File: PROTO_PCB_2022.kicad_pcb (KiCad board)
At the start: 2 copper layers, 81.4 x 40.6 mm, 30 parts, among them J1 HORN_EN1, J10 ECU_3, J11 12V_IN, J12 12V_OUT_EXTRA, J2 HORN_CONN, J3 STARTER_MOTOR_EN, J4 VESC_EN_SIGNAL, J5 ECU_POWER_DIST, J6 BRAKELIGHTS_EN1, J7 BRAKELIGHTS_CONN, J8 ECU_1, J9 ECU_2, Q1 HORN_MOSFET1, Q2 BRAKELIGHTS_MOSFET1, U1 LD1117S50TR_SOT223

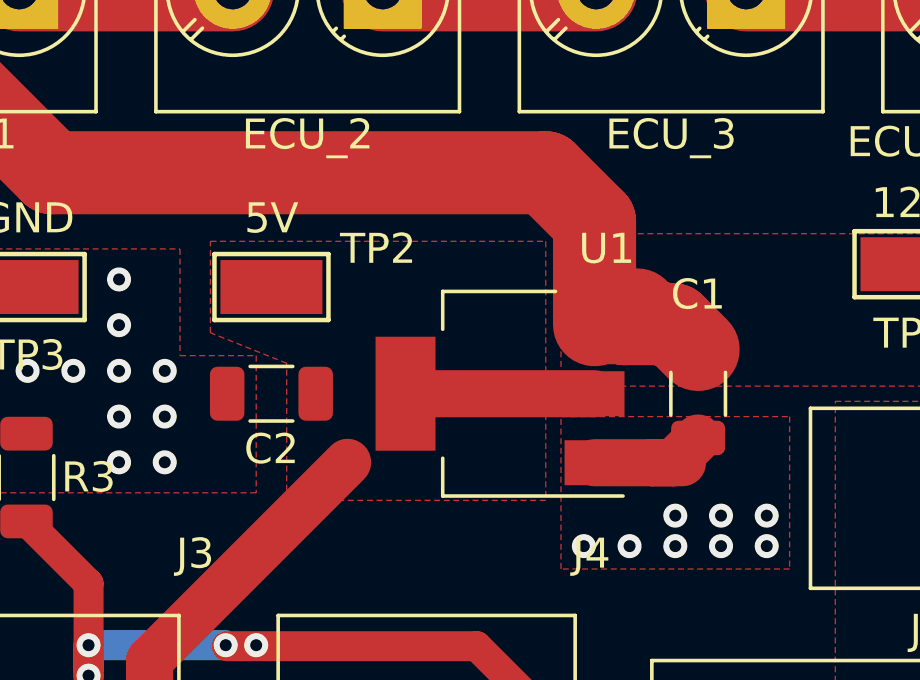
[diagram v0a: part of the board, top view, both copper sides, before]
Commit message: final design with gerbers
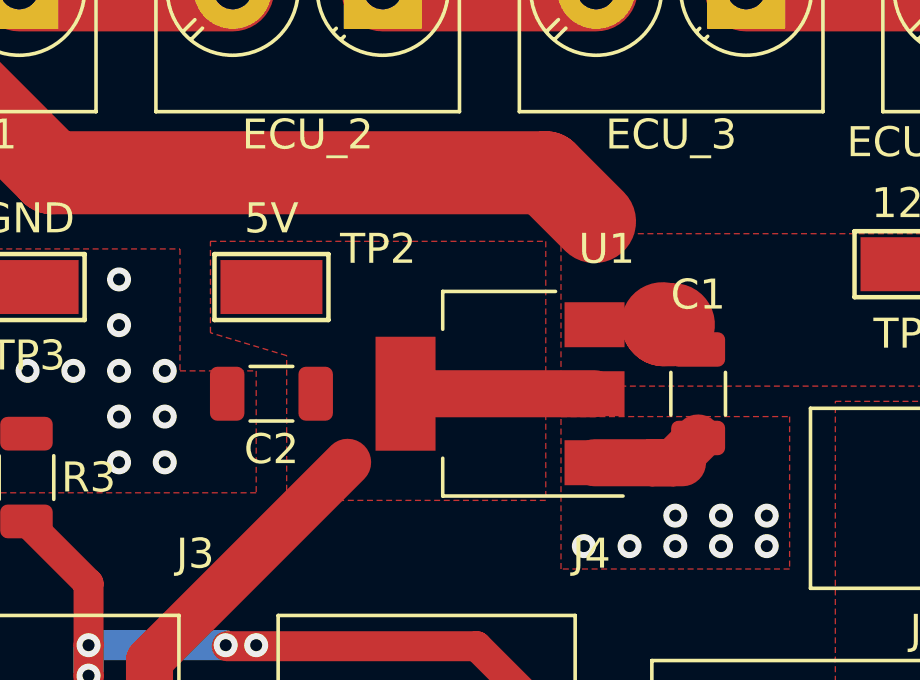
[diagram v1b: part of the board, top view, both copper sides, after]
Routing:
- net 12V_FOR_BRAKELIGHTS: track 68.5 -> 60.1 mm

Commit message: schematic done
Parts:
- removed the J1 at (95.5, 112.4)
- removed R5: 10k, Resistor_SMD:R_1206_3216Metric
- added F2: 5A, Fuse:Fuseholder_Blade_Mini_Keystone_3568, F.Cu at (84.4, 127.1)
- added F3: 2A, Fuse:Fuseholder_Blade_Mini_Keystone_3568, F.Cu at (84.4, 134.7)
- added F4: 2A, Fuse:Fuseholder_Blade_Mini_Keystone_3568, F.Cu at (105.9, 127.1)
- added F5: 1A, Fuse:Fuseholder_Blade_Mini_Keystone_3568, F.Cu at (84.4, 142.2)
- added F6: 1A, Fuse:Fuseholder_Blade_Mini_Keystone_3568, F.Cu at (105.9, 134.7)
- added F7: 1A, Fuse:Fuseholder_Blade_Mini_Keystone_3568, F.Cu at (84.4, 149.8)
- added H3: MountingHole, MountingHole:MountingHole_3.2mm_M3, F.Cu at (95.4, 158.2)
- added H4: MountingHole, MountingHole:MountingHole_3.2mm_M3, F.Cu at (95.4, 165.2)
- added J11: SW_START, Connector_Molex:Molex_Micro-Fit_3.0_43650-0200_1x02_P3.00mm_Horizontal, F.Cu at (149.2, 140.8)
- added J13: 5V_OUT_AUX, Connector_Molex:Molex_Micro-Fit_3.0_43650-0200_1x02_P3.00mm_Horizontal, F.Cu at (149.2, 154.3)
- D1, D2: footprint Resistor_SMD:R_0603_1608Metric -> LED_SMD:LED_1206_3216Metric
- F1: value Fuse -> 10A; footprint Fuse:Fuseholder_Blade_ATO_Littelfuse_Pudenz_2_Pin -> Fuse:Fuseholder_Blade_Mini_Keystone_3568
- H1, H2: footprint MountingHole:MountingHole_2.7mm_M2.5 -> MountingHole:MountingHole_3.2mm_M3
- J1: renamed from J11; value 12V_IN -> 12V_BATT; footprint TerminalBlock_Phoenix:TerminalBlock_Phoenix_PT-1,5-2-5.0-H_1x02_P5.00mm_Horizontal -> Connector_Molex:Molex_Micro-Fit_3.0_43650-0200_1x02_P3.00mm_Horizontal
- J10: value ECU_3 -> 12V_OUT_AUX; footprint TerminalBlock_Phoenix:TerminalBlock_Phoenix_PT-1,5-2-5.0-H_1x02_P5.00mm_Horizontal -> Connector_Molex:Molex_Micro-Fit_3.0_43650-0200_1x02_P3.00mm_Horizontal
- J12: value 12V_OUT_EXTRA -> VESC_START; footprint TerminalBlock_Phoenix:TerminalBlock_Phoenix_PT-1,5-2-5.0-H_1x02_P5.00mm_Horizontal -> Connector_Molex:Molex_Micro-Fit_3.0_43650-0200_1x02_P3.00mm_Horizontal
- J2: value HORN_CONN -> SW_KILL_DRIVER; footprint TerminalBlock_Phoenix:TerminalBlock_Phoenix_PT-1,5-2-5.0-H_1x02_P5.00mm_Horizontal -> Connector_Molex:Molex_Micro-Fit_3.0_43650-0200_1x02_P3.00mm_Horizontal
- J3: value STARTER_MOTOR_EN -> SW_KILL_LEFT; footprint footprints:436500201 -> Connector_Molex:Molex_Micro-Fit_3.0_43650-0200_1x02_P3.00mm_Horizontal
- J4: value VESC_EN_SIGNAL -> SW_KILL_RIGHT; footprint footprints:436500201 -> Connector_Molex:Molex_Micro-Fit_3.0_43650-0200_1x02_P3.00mm_Horizontal
- J5: value ECU_POWER_DIST -> ECU_POWER; footprint TerminalBlock_Phoenix:TerminalBlock_Phoenix_PT-1,5-2-5.0-H_1x02_P5.00mm_Horizontal -> Connector_Molex:Molex_Micro-Fit_3.0_43650-0200_1x02_P3.00mm_Horizontal
- J6: value BRAKELIGHTS_EN1 -> SW_BRAKE; footprint footprints:436500201 -> Connector_Molex:Molex_Micro-Fit_3.0_43650-0200_1x02_P3.00mm_Horizontal
- J7: value BRAKELIGHTS_CONN -> 12V_OUT_HORN; footprint TerminalBlock_Phoenix:TerminalBlock_Phoenix_PT-1,5-2-5.0-H_1x02_P5.00mm_Horizontal -> Connector_Molex:Molex_Micro-Fit_3.0_43650-0200_1x02_P3.00mm_Horizontal
- J8: value ECU_1 -> BRAKELIGHT_POWER; footprint TerminalBlock_Phoenix:TerminalBlock_Phoenix_PT-1,5-2-5.0-H_1x02_P5.00mm_Horizontal -> Connector_Molex:Molex_Micro-Fit_3.0_43650-0200_1x02_P3.00mm_Horizontal
- J9: value ECU_2 -> 12V_OUT_TEL; footprint TerminalBlock_Phoenix:TerminalBlock_Phoenix_PT-1,5-2-5.0-H_1x02_P5.00mm_Horizontal -> Connector_Molex:Molex_Micro-Fit_3.0_43650-0200_1x02_P3.00mm_Horizontal
- Q1: value HORN_MOSFET1 -> MOSFET_ECU
- Q2: value BRAKELIGHTS_MOSFET1 -> MOSFET_BRAKE_LIGHT
- R1: value 4.7k -> 1k
- R3: value 10k -> 1k
- R4: value 4.7k -> 10k
- moved J4 84.4 mm to (42.8, 141.6), turned to 0 degrees
- moved J1 82.7 mm to (208.7, 129.9)
- moved TP1 82.7 mm to (214.8, 112.6)
- moved J5 79.5 mm to (184.2, 151.6), turned to 0 degrees
- moved D2 77.5 mm to (101.0, 171.2), turned to 0 degrees
- moved Q2 75.9 mm to (111.2, 168.9)
- moved R4 75.9 mm to (92.2, 170.3), turned to 0 degrees
- moved J7 75.9 mm to (143.2, 127.3), turned to 0 degrees
- moved Q1 74.1 mm to (106.8, 168.9)
- moved J8 72.9 mm to (121.6, 155.9), turned to 0 degrees
- moved C2 72.6 mm to (185.3, 96.0)
- moved D1 72.0 mm to (97.0, 171.2), turned to 0 degrees
- moved R2 70.7 mm to (86.6, 169.9)
- moved J2 70.4 mm to (32.0, 121.5), turned to 0 degrees
- moved R1 69.9 mm to (81.0, 169.9), turned to 0 degrees
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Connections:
- C1 pad 1: 12V_FOR_BRAKELIGHTS -> +12V
- D1 pad 2: HORN_EN_5V -> Net-(D1-Pad2)
- D2 pad 2: BRAKELIGHTS_EN_5V -> Net-(D2-Pad2)
- F1 pad 1: BATT_12V -> +12V
- F1 pad 2: 12V_FOR_BRAKELIGHTS -> Net-(F1-Pad2)
- J1 pad 1: GND -> Net-(F1-Pad2)
- J1 pad 2: BATT_12V -> GND
- J10 pad 1: ECU_KILL_EN_TOGGLESWITCH_3B -> GND
- J10 pad 2: ECU_KILL_EN_TOGGLESWITCH_2B -> Net-(F6-Pad1)
- J12 pad 1: GND -> Net-(J11-Pad2)
- J12 pad 2: 12V_FOR_BRAKELIGHTS -> Net-(J11-Pad1)
- J2 pad 1: HORN_GND -> +5V
- J2 pad 2: 12V_FOR_BRAKELIGHTS -> Net-(J2-Pad2)
- J3 pad 1: VESC_EN_5V -> Net-(J2-Pad2)
- J3 pad 2: +5V -> Net-(J3-Pad2)
- J4 pad 1: GND -> Net-(J3-Pad2)
- J4 pad 2: VESC_EN_5V -> Net-(D1-Pad2)
- J5 pad 1: GND -> Net-(J5-Pad1)
- J5 pad 2: ECU_KILL_EN_TOGGLESWITCH_3B -> Net-(F2-Pad1)
- J6 pad 1: BRAKELIGHTS_EN_5V -> +5V
- J6 pad 2: +5V -> Net-(D2-Pad2)
- J7 pad 1: BRAKELIGHTS_GND -> GND
- J7 pad 2: 12V_FOR_BRAKELIGHTS -> Net-(F3-Pad1)
- J8 pad 1: ECU_KILL_EN_TOGGLESWITCH_1B -> Net-(J8-Pad1)
- J8 pad 2: 12V_FOR_BRAKELIGHTS -> Net-(F4-Pad1)
- J9 pad 1: ECU_KILL_EN_TOGGLESWITCH_2B -> GND
- J9 pad 2: ECU_KILL_EN_TOGGLESWITCH_1B -> Net-(F5-Pad1)
- Q1 pad 1: HORN_GND -> Net-(J5-Pad1)
- Q1 pad 2: HORN_EN_5V -> Net-(D1-Pad2)
- Q2 pad 1: BRAKELIGHTS_GND -> Net-(J8-Pad1)
- Q2 pad 2: BRAKELIGHTS_EN_5V -> Net-(D2-Pad2)
- R2 pad 1: HORN_EN_5V -> Net-(D1-Pad2)
- R3 pad 1: VESC_EN_5V -> Net-(D2-Pad1)
- R4 pad 1: Net-(D2-Pad1) -> Net-(D2-Pad2)
- TP1 pad 1: 12V_FOR_BRAKELIGHTS -> +12V
- U1 pad 3: 12V_FOR_BRAKELIGHTS -> +12V
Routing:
- net +5V: track 66.4 -> 0.00 mm
- net 12V_FOR_BRAKELIGHTS: track 60.1 -> 0.00 mm
- net HORN_EN_5V: track 31.6 -> 0.00 mm
- net BRAKELIGHTS_EN_5V: track 31.3 -> 0.00 mm, vias 4 -> 0
- net VESC_EN_5V: track 28.3 -> 0.00 mm, vias 4 -> 0
- net GND: track 21.3 -> 0.00 mm, vias 27 -> 0
- net BRAKELIGHTS_GND: track 15.2 -> 0.00 mm
- net HORN_GND: track 10.3 -> 0.00 mm
- net ECU_KILL_EN_TOGGLESWITCH_3B: track 7.12 -> 0.00 mm
- net ECU_KILL_EN_TOGGLESWITCH_2B: track 7.12 -> 0.00 mm
- net ECU_KILL_EN_TOGGLESWITCH_1B: track 7.12 -> 0.00 mm
- net Net-(D2-Pad1): track 4.33 -> 0.00 mm
- net Net-(D1-Pad1): track 4.25 -> 0.00 mm
- removed copper zone on F.Cu, net +5V
- removed copper zone on F.Cu, net 12V_FOR_BRAKELIGHTS
- removed copper zone on F.Cu, net BATT_12V
- removed copper zone on B.Cu, net GND
- removed copper zone on F.Cu, net GND
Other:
- board text removed: "5V"
- board text removed: "GND"
- board text removed: "HORN"
- board text removed: "LIGHTS"

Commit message: finished PCB layout
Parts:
- J1: footprint Connector_Molex:Molex_Micro-Fit_3.0_43650-0200_1x02_P3.00mm_Horizontal -> TerminalBlock_Phoenix:TerminalBlock_Phoenix_PT-1,5-2-5.0-H_1x02_P5.00mm_Horizontal
- moved J1 153.0 mm to (55.9, 121.8), turned to 270 degrees
- moved TP1 151.2 mm to (64.3, 127.0)
- moved H1 140.9 mm to (54.0, 104.0)
- moved F1 133.5 mm to (63.8, 138.2), turned to 180 degrees
- moved TP3 108.3 mm to (64.3, 120.1)
- moved J5 83.5 mm to (111.6, 110.2)
- moved J7 82.3 mm to (62.7, 110.2)
- moved J2 77.3 mm to (107.2, 139.7), turned to 180 degrees
- moved H3 74.1 mm to (146.0, 104.0)
- moved J10 72.9 mm to (86.1, 110.2)
- moved J9 68.2 mm to (74.4, 110.2)
- moved J13 67.7 mm to (97.8, 110.2)
- moved R4 66.1 mm to (146.6, 132.6), turned to 270 degrees
- moved C1 57.1 mm to (137.9, 122.2)
- moved H4 54.1 mm to (146.0, 146.0)
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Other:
- board size 81.4 x 40.6 mm -> 100 x 50 mm

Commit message: did some more layout work
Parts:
- removed F6, F7: 1A, Fuse:Fuseholder_Blade_Mini_Keystone_3568
- removed J10: 12V_OUT_AUX, Connector_Molex:Molex_Micro-Fit_3.0_43650-0200_1x02_P3.00mm_Horizontal
- removed J13: 5V_OUT_AUX, Connector_Molex:Molex_Micro-Fit_3.0_43650-0200_1x02_P3.00mm_Horizontal
- J9: value 12V_OUT_TEL -> 12V_OUT_AUX
- moved R2 49.5 mm to (112.5, 121.9), turned to 0 degrees
- moved R3 45.0 mm to (97.0, 129.0), turned to 90 degrees
- moved Q1 44.9 mm to (112.3, 117.6)
- moved R4 33.8 mm to (112.8, 132.1), turned to 180 degrees
- moved Q2 28.5 mm to (112.5, 127.0)
- moved TP3 26.4 mm to (59.2, 146.1), turned to 270 degrees
- moved F1 26.0 mm to (57.1, 113.0), turned to 270 degrees
- moved R1 24.9 mm to (84.6, 129.2), turned to 270 degrees
- moved C2 23.5 mm to (123.4, 118.6)
- moved J5 22.7 mm to (88.9, 110.0)
- moved F2 22.4 mm to (92.5, 118.6)
- moved J8 21.8 mm to (101.3, 110.0)
- moved F4 21.6 mm to (104.6, 118.4)
- moved TP1 21.3 mm to (58.7, 106.4), turned to 270 degrees
- moved J12 20.8 mm to (114.0, 110.0)
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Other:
- board size 100 x 50 mm -> 80 x 50 mm

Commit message: even more layout changes
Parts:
- removed F1: 10A, Fuse:Fuseholder_Blade_Mini_Keystone_3568
- added D3: LED, LED_SMD:LED_1206_3216Metric, F.Cu at (144.8, 116.1)
- added R5: 1k, Resistor_SMD:R_1206_3216Metric, F.Cu at (144.7, 119.4)
- moved TP3 34.6 mm to (58.4, 111.5)
- moved J1 8.89 mm to (56.1, 122.9)
- moved TP1 7.01 mm to (53.8, 111.5)
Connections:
- J1 pad 1: Net-(F1-Pad2) -> +12V
- J11 pad 2: Net-(J11-Pad2) -> Net-(D3-Pad2)
- J12 pad 1: Net-(J11-Pad2) -> Net-(J12-Pad1)

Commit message: finishes schematic, footprint assignment, and BOM
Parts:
- removed C1: 1u, Capacitor_SMD:C_1206_3216Metric
- removed C2: 4.7u, Capacitor_SMD:C_1206_3216Metric
- removed the TP2 at (125.7, 112.8)
- removed U1: LD1117S50TR_SOT223, Package_TO_SOT_SMD:SOT-223-3_TabPin2
- added F5: 1A, Fuse:Fuseholder_Blade_Mini_Keystone_3568, F.Cu at (185.7, 132.6)
- added J10: 12V_AUX, Connector_Molex:Molex_Micro-Fit_3.0_43650-0200_1x02_P3.00mm_Horizontal, F.Cu at (186.2, 148.4)
- added L2: RED, LED_SMD:LED_1206_3216Metric, F.Cu at (202.3, 131.8)
- added R1: 1k, Resistor_SMD:R_1206_3216Metric, F.Cu at (184.7, 152.0)
- J1: value 12V_BATT -> 12V_IN; footprint TerminalBlock_Phoenix:TerminalBlock_Phoenix_PT-1,5-2-5.0-H_1x02_P5.00mm_Horizontal -> Footprint Library:MOLEX_2002411212
- J5: value ECU_POWER -> 12V_ECU
- J6: renamed from J7; value 12V_OUT_HORN -> 12V_HORN
- J8: renamed from J9; value 12V_OUT_AUX -> 12V_TEL
- J9: renamed from J8; value BRAKELIGHT_POWER -> 12V_BRAKE_LIGHT
- L1: renamed from D1; value LED -> GREEN
- L3: renamed from D2; value LED -> GREEN
- L4: renamed from D3; value LED -> GREEN
- Q1, Q2: footprint Package_TO_SOT_SMD:SOT-23 -> Package_TO_SOT_SMD:TO-252-3_TabPin2
- TP1: value TestPoint -> 12V Test
- TP2: renamed from TP3; value TestPoint -> GND Test
- moved J1 120.9 mm to (176.4, 135.4), turned to 0 degrees
- moved Q2 60.3 mm to (165.1, 97.5)
- moved Q1 43.4 mm to (154.7, 108.2)
- renumbered F2 to F1, F3 to F2, F5 to F3, J6 to J7, R1 to R2, R2 to R3, R3 to R4, R4 to R5, R5 to R6
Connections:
- J2 pad 1: +5V -> +12V
- J7 pad 1: +5V -> +12V

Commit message: new layout
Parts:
- R6: value 1k -> 100
- moved L2 150.5 mm to (52.5, 146.7)
- moved R1 132.5 mm to (52.5, 142.9), turned to 180 degrees
- moved J10 120.9 mm to (71.3, 111.0)
- moved J1 115.4 mm to (61.3, 126.4), turned to 270 degrees
- moved Q1 109.6 mm to (48.6, 135.9), turned to 180 degrees
- moved F5 104.9 mm to (81.7, 118.7), turned to 270 degrees
- moved R3 56.9 mm to (57.1, 134.6)
- moved Q2 54.9 mm to (115.3, 120.7)
- moved TP1 35.5 mm to (58.8, 146.7), turned to 0 degrees
- moved L1 34.0 mm to (57.0, 137.8)
- moved TP2 31.4 mm to (58.8, 142.9), turned to 0 degrees
- moved J5 29.1 mm to (59.8, 111.0)
- moved R2 24.2 mm to (61.3, 136.1), turned to 90 degrees
- moved L4 24.2 mm to (121.7, 123.2), turned to 270 degrees
- moved R6 23.2 mm to (121.7, 117.5), turned to 90 degrees
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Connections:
- Q1 pad 1: Net-(J5-Pad1) -> Net-(J4-Pad2)
- Q1 pad 2: Net-(J4-Pad2) -> Net-(J5-Pad1)
- Q2 pad 1: Net-(J9-Pad1) -> Net-(J7-Pad2)
- Q2 pad 2: Net-(J7-Pad2) -> Net-(J9-Pad1)
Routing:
- net Net-(J5-Pad1): track 0.00 -> 58.6 mm
- net GND: track 0.00 -> 42.5 mm, vias 0 -> 11
- net Net-(J11-Pad1): track 0.00 -> 33.3 mm
- net Net-(J7-Pad2): track 0.00 -> 26.8 mm
- net Net-(J9-Pad1): track 0.00 -> 24.2 mm
- net Net-(J4-Pad2): track 0.00 -> 19.0 mm
- net Net-(J11-Pad2): track 0.00 -> 16.1 mm
- net Net-(J3-Pad2): track 0.00 -> 8.66 mm
- net Net-(J2-Pad2): track 0.00 -> 8.45 mm
- net Net-(J12-Pad1): track 0.00 -> 7.58 mm
- net Net-(L2-Pad1): track 0.00 -> 3.84 mm
- net Net-(L3-Pad1): track 0.00 -> 3.23 mm
- net Net-(L1-Pad1): track 0.00 -> 3.02 mm
- net Net-(L4-Pad1): track 0.00 -> 2.85 mm
- added copper zone on F.Cu, net +12V
- added copper zone on B.Cu, net GND
- added copper zone on F.Cu, net Net-(F1-Pad1)
- added copper zone on F.Cu, net Net-(F2-Pad1)
- added copper zone on F.Cu, net Net-(F3-Pad1)
- added copper zone on F.Cu, net Net-(F4-Pad1)
- added copper zone on F.Cu, net Net-(F5-Pad1)
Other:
- board size 80 x 50 mm -> 90.8 x 50.2 mm
- board text added: "GND"

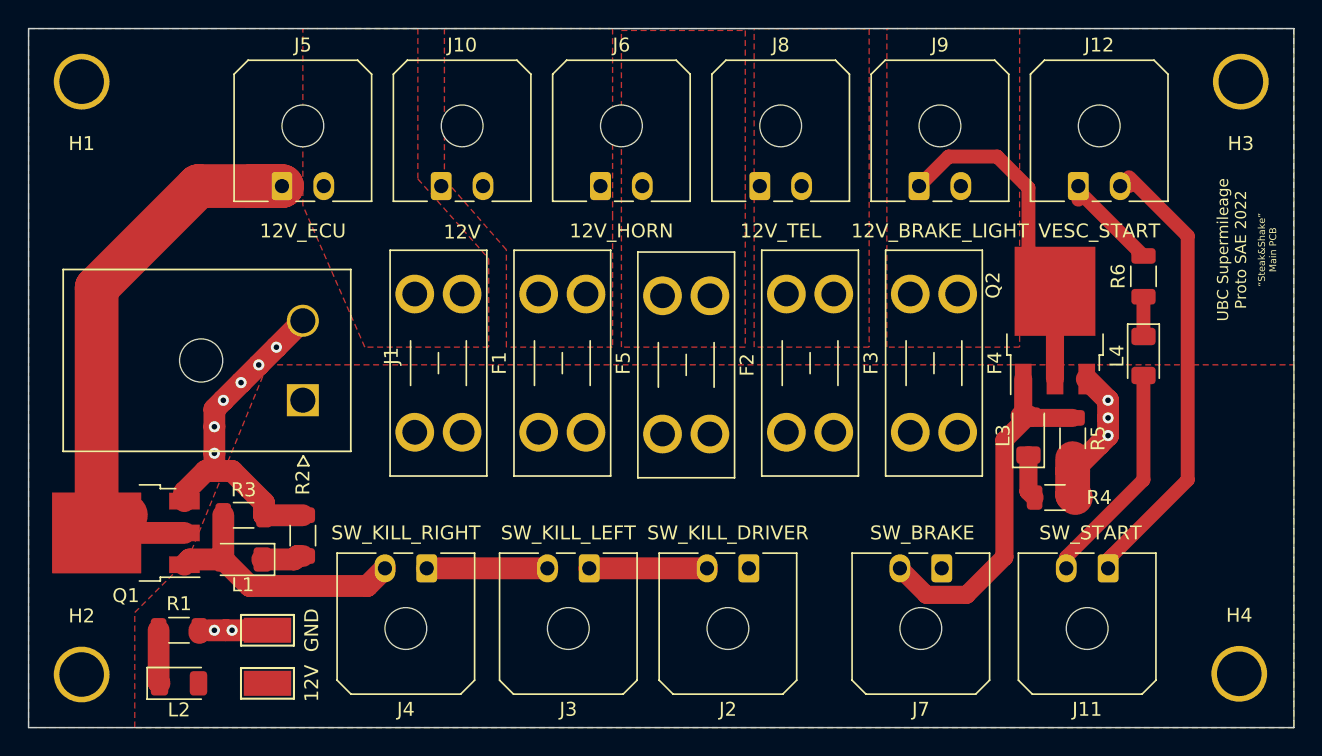
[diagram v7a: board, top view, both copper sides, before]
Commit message: updates silkscreen and minor tracing
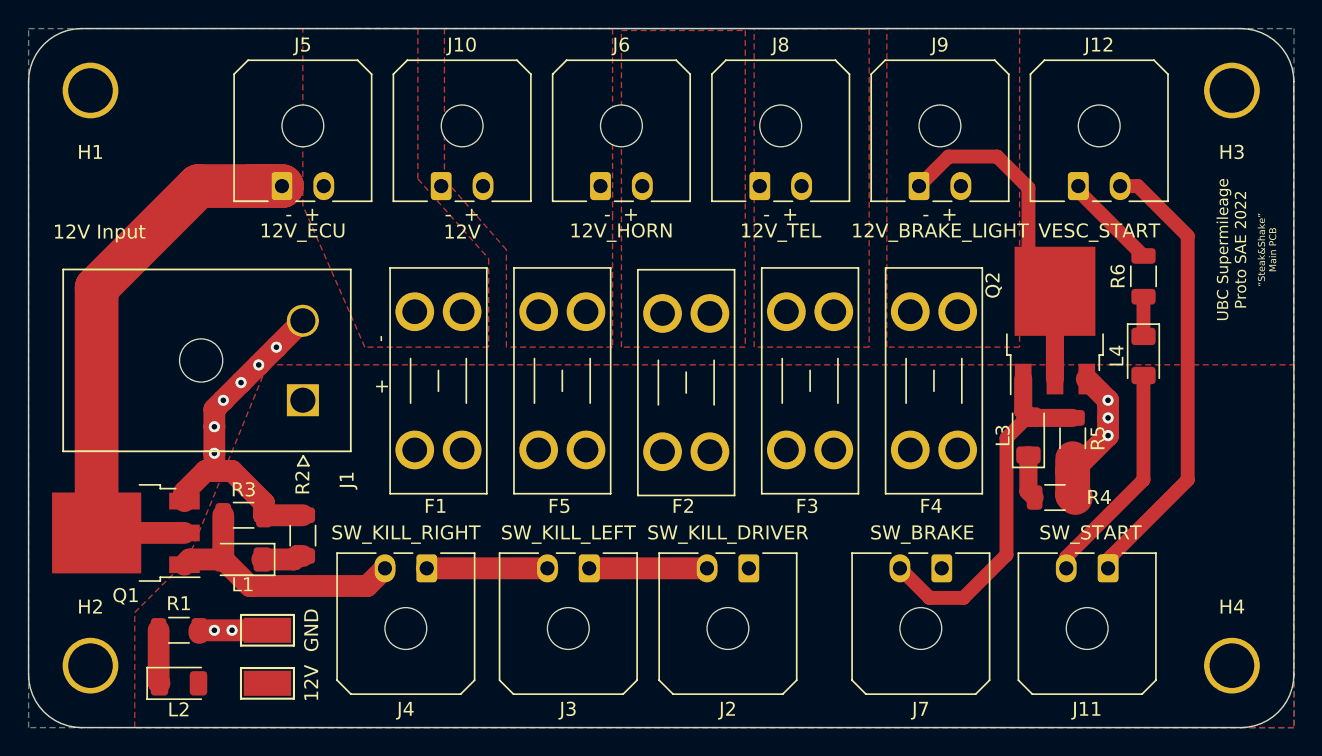
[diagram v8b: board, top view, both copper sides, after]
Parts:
- moved F1 1.27 mm to (72.8, 120.0)
- moved F2 1.27 mm to (90.6, 120.1)
- moved F3 1.27 mm to (99.4, 120.0)
- moved F4 1.27 mm to (108.3, 120.0)
- moved F5 1.27 mm to (81.7, 120.0)
- moved H3 0.90 mm to (128.0, 104.1)
- moved H2 0.90 mm to (46.1, 145.4)
- moved H1 0.90 mm to (46.1, 104.1)
- moved H4 0.79 mm to (128.0, 145.4)
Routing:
- net Net-(J5-Pad1): track 58.6 -> 56.8 mm
- net Net-(J12-Pad1): track 7.58 -> 6.61 mm
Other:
- outline, holes or cut-outs redrawn
- board text added: "- +"
- board text added: "12V Input"
